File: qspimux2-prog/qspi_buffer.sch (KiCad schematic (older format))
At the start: 31 parts, among them J201 Conn_01x10_MountingPin, U201 SN74LVC1T45DCK, U202 SN74LVC1T45DCK, U203 SN74LVC1T45DCK, U204 SN74LVC1T45DCK, U205 SN74LVC1T45DCK, U206 SN74LVC1T45DCK, U207 SN74LVC1T45DCK

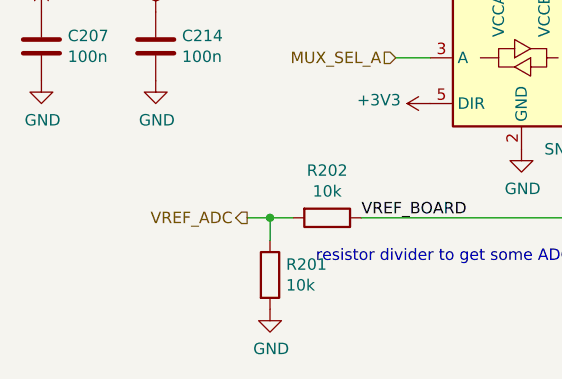
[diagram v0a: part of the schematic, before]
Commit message: add a few missing capacitors and do some slight layout optimizations
add two missing capacitors on the supply rails of the microcontroller
add capacitor to vtarget monitoringto get a low pass
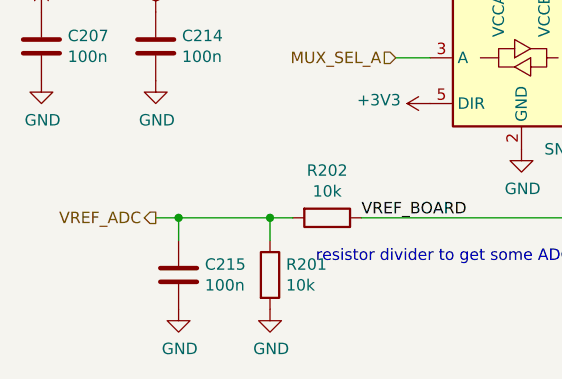
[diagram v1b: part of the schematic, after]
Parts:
- added C215: 100n, Capacitor_SMD:C_0402_1005Metric, symbol Device:C
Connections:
- net GND: now also C215.2
- net VREF_ADC: now also C215.1
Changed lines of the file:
@@
 $EndDescr
 $Comp
-L power:+3V3 #PWR0236
+L power:+3V3 #PWR0237
 U 1 1 5DE94518
 P 8300 5100
-F 0 "#PWR0236" H 8300 4950 50  0001 C CNN
+F 0 "#PWR0237" H 8300 4950 50  0001 C CNN
 F 1 "+3V3" H 8315 5273 50  0000 C CNN
 F 2 "" H 8300 5100 50  0001 C CNN
@@
 $EndComp
 $Comp
-L power:+3V3 #PWR0233
+L power:+3V3 #PWR0234
 U 1 1 5DE8F4FA
 P 8300 1200
-F 0 "#PWR0233" H 8300 1050 50  0001 C CNN
+F 0 "#PWR0234" H 8300 1050 50  0001 C CNN
 F 1 "+3V3" H 8315 1373 50  0000 C CNN
 F 2 "" H 8300 1200 50  0001 C CNN
@@
 $EndComp
 $Comp
-L power:VDD #PWR0253
+L power:VDD #PWR0254
 U 1 1 5DE9D1E1
 P 8500 9000
-F 0 "#PWR0253" H 8500 8850 50  0001 C CNN
+F 0 "#PWR0254" H 8500 8850 50  0001 C CNN
 F 1 "VDD" H 8517 9173 50  0000 C CNN
 F 2 "" H 8500 9000 50  0001 C CNN
@@
 $EndComp
 $Comp
-L power:+3V3 #PWR0234
+L power:+3V3 #PWR0235
 U 1 1 5DE91572
 P 8300 2500
-F 0 "#PWR0234" H 8300 2350 50  0001 C CNN
+F 0 "#PWR0235" H 8300 2350 50  0001 C CNN
 F 1 "+3V3" H 8315 2673 50  0000 C CNN
 F 2 "" H 8300 2500 50  0001 C CNN
@@
 $EndComp
 $Comp
-L power:VDD #PWR0252
+L power:VDD #PWR0253
 U 1 1 5DE99677
 P 8500 7700
-F 0 "#PWR0252" H 8500 7550 50  0001 C CNN
+F 0 "#PWR0253" H 8500 7550 50  0001 C CNN
 F 1 "VDD" H 8517 7873 50  0000 C CNN
 F 2 "" H 8500 7700 50  0001 C CNN
@@
 $EndComp
 $Comp
-L power:GND #PWR0241
+L power:GND #PWR0242
 U 1 1 5DEB0DC4
 P 8400 3300
-F 0 "#PWR0241" H 8400 3050 50  0001 C CNN
+F 0 "#PWR0242" H 8400 3050 50  0001 C CNN
 F 1 "GND" H 8405 3127 50  0000 C CNN
 F 2 "" H 8400 3300 50  0001 C CNN
@@
 $EndComp
 $Comp
-L power:GND #PWR0244
+L power:GND #PWR0245
 U 1 1 5E26BF26
 P 8400 7200
-F 0 "#PWR0244" H 8400 6950 50  0001 C CNN
+F 0 "#PWR0245" H 8400 6950 50  0001 C CNN
 F 1 "GND" H 8405 7027 50  0000 C CNN
 F 2 "" H 8400 7200 50  0001 C CNN
@@
 $EndComp
 $Comp
-L power:VDD #PWR0249
+L power:VDD #PWR0250
 U 1 1 5DE9300A
 P 8500 3800
-F 0 "#PWR0249" H 8500 3650 50  0001 C CNN
+F 0 "#PWR0250" H 8500 3650 50  0001 C CNN
 F 1 "VDD" H 8517 3973 50  0000 C CNN
 F 2 "" H 8500 3800 50  0001 C CNN
@@
 $EndComp
 $Comp
-L power:+3V3 #PWR0235
+L power:+3V3 #PWR0236
 U 1 1 5DE92FFC
 P 8300 3800
-F 0 "#PWR0235" H 8300 3650 50  0001 C CNN
+F 0 "#PWR0236" H 8300 3650 50  0001 C CNN
 F 1 "+3V3" H 8315 3973 50  0000 C CNN
 F 2 "" H 8300 3800 50  0001 C CNN
@@
 $EndComp
 $Comp
-L power:GND #PWR0242
+L power:GND #PWR0243
 U 1 1 5DEB8F33
 P 8400 4600
-F 0 "#PWR0242" H 8400 4350 50  0001 C CNN
+F 0 "#PWR0243" H 8400 4350 50  0001 C CNN
 F 1 "GND" H 8405 4427 50  0000 C CNN
 F 2 "" H 8400 4600 50  0001 C CNN
@@
 $EndComp
 $Comp
-L power:VDD #PWR0247
+L power:VDD #PWR0248
 U 1 1 5DE90785
 P 8500 1200
-F 0 "#PWR0247" H 8500 1050 50  0001 C CNN
+F 0 "#PWR0248" H 8500 1050 50  0001 C CNN
 F 1 "VDD" H 8517 1373 50  0000 C CNN
 F 2 "" H 8500 1200 50  0001 C CNN
@@
 $EndComp
 $Comp
-L power:+3V3 #PWR0237
+L power:+3V3 #PWR0238
 U 1 1 5DE971AE
 P 8300 6400
-F 0 "#PWR0237" H 8300 6250 50  0001 C CNN
+F 0 "#PWR0238" H 8300 6250 50  0001 C CNN
 F 1 "+3V3" H 8315 6573 50  0000 C CNN
 F 2 "" H 8300 6400 50  0001 C CNN
@@
 $EndComp
 $Comp
-L power:VDD #PWR0248
+L power:VDD #PWR0249
 U 1 1 5DE91580
 P 8500 2500
-F 0 "#PWR0248" H 8500 2350 50  0001 C CNN
+F 0 "#PWR0249" H 8500 2350 50  0001 C CNN
 F 1 "VDD" H 8517 2673 50  0000 C CNN
 F 2 "" H 8500 2500 50  0001 C CNN
@@
 $EndComp
 $Comp
-L power:GND #PWR0240
+L power:GND #PWR0241
 U 1 1 5DE8B08B
 P 8400 2000
-F 0 "#PWR0240" H 8400 1750 50  0001 C CNN
+F 0 "#PWR0241" H 8400 1750 50  0001 C CNN
 F 1 "GND" H 8405 1827 50  0000 C CNN
 F 2 "" H 8400 2000 50  0001 C CNN
@@
 $EndComp
 $Comp
-L power:VDD #PWR0250
+L power:VDD #PWR0251
 U 1 1 5DE94526
 P 8500 5100
-F 0 "#PWR0250" H 8500 4950 50  0001 C CNN
+F 0 "#PWR0251" H 8500 4950 50  0001 C CNN
 F 1 "VDD" H 8517 5273 50  0000 C CNN
 F 2 "" H 8500 5100 50  0001 C CNN
@@
 $EndComp
 $Comp
-L power:GND #PWR0243
+L power:GND #PWR0244
 U 1 1 5DEB94D5
 P 8400 5900
-F 0 "#PWR0243" H 8400 5650 50  0001 C CNN
+F 0 "#PWR0244" H 8400 5650 50  0001 C CNN
 F 1 "GND" H 8405 5727 50  0000 C CNN
 F 2 "" H 8400 5900 50  0001 C CNN
@@
 $EndComp
 $Comp
-L power:GND #PWR0245
+L power:GND #PWR0246
 U 1 1 5DEC9D31
 P 8400 8500
-F 0 "#PWR0245" H 8400 8250 50  0001 C CNN
+F 0 "#PWR0246" H 8400 8250 50  0001 C CNN
 F 1 "GND" H 8405 8327 50  0000 C CNN
 F 2 "" H 8400 8500 50  0001 C CNN
@@
 $EndComp
 $Comp
-L power:VDD #PWR0251
+L power:VDD #PWR0252
 U 1 1 5DE971BC
 P 8500 6400
-F 0 "#PWR0251" H 8500 6250 50  0001 C CNN
+F 0 "#PWR0252" H 8500 6250 50  0001 C CNN
 F 1 "VDD" H 8517 6573 50  0000 C CNN
 F 2 "" H 8500 6400 50  0001 C CNN
@@
 $EndComp
 $Comp
-L power:+3V3 #PWR0238
+L power:+3V3 #PWR0239
 U 1 1 5DE99669
 P 8300 7700
-F 0 "#PWR0238" H 8300 7550 50  0001 C CNN
+F 0 "#PWR0239" H 8300 7550 50  0001 C CNN
 F 1 "+3V3" H 8315 7873 50  0000 C CNN
 F 2 "" H 8300 7700 50  0001 C CNN
@@
 $EndComp
 $Comp
-L power:GND #PWR0246
+L power:GND #PWR0247
 U 1 1 5DECAA79
 P 8400 9800
-F 0 "#PWR0246" H 8400 9550 50  0001 C CNN
+F 0 "#PWR0247" H 8400 9550 50  0001 C CNN
 F 1 "GND" H 8405 9627 50  0000 C CNN
 F 2 "" H 8400 9800 50  0001 C CNN
@@
 $EndComp
 $Comp
-L power:+3V3 #PWR0239
+L power:+3V3 #PWR0240
 U 1 1 5DE9D1D3
 P 8300 9000
-F 0 "#PWR0239" H 8300 8850 50  0001 C CNN
+F 0 "#PWR0240" H 8300 8850 50  0001 C CNN
 F 1 "+3V3" H 8315 9173 50  0000 C CNN
 F 2 "" H 8300 9000 50  0001 C CNN
@@
 $EndComp
 $Comp
-L power:+3V3 #PWR0232
+L power:+3V3 #PWR0233
 U 1 1 5E06B1B2
 P 8000 9600
-F 0 "#PWR0232" H 8000 9450 50  0001 C CNN
+F 0 "#PWR0233" H 8000 9450 50  0001 C CNN
 F 1 "+3V3" V 8015 9728 50  0000 L CNN
 F 2 "" H 8000 9600 50  0001 C CNN
@@
 $EndComp
 $Comp
-L power:+3V3 #PWR0230
+L power:+3V3 #PWR0231
 U 1 1 5E054678
 P 8000 1800
-F 0 "#PWR0230" H 8000 1650 50  0001 C CNN
+F 0 "#PWR0231" H 8000 1650 50  0001 C CNN
 F 1 "+3V3" V 8015 1928 50  0000 L CNN
 F 2 "" H 8000 1800 50  0001 C CNN
@@
 $EndComp
 $Comp
-L power:GND #PWR0229
+L power:GND #PWR0230
 U 1 1 5E230D27
 P 7300 10500
-F 0 "#PWR0229" H 7300 10250 50  0001 C CNN
+F 0 "#PWR0230" H 7300 10250 50  0001 C CNN
 F 1 "GND" H 7305 10327 50  0000 C CNN
 F 2 "" H 7300 10500 50  0001 C CNN
@@
 	10400 10100 7700 10100
 Wire Wire Line
-	7200 10100 7300 10100
+	6800 10100 6900 10100
 Wire Wire Line
 	7900 8300 8000 8300
@@
 $EndComp
 $Comp
-L power:GND #PWR0256
+L power:GND #PWR0257
 U 1 1 5DEECC05
 P 11200 6900
-F 0 "#PWR0256" H 11200 6650 50  0001 C CNN
+F 0 "#PWR0257" H 11200 6650 50  0001 C CNN
 F 1 "GND" H 11205 6727 50  0000 C CNN
 F 2 "" H 11200 6900 50  0001 C CNN
@@
 $EndComp
 $Comp
-L power:+3V3 #PWR0231
+L power:+3V3 #PWR0232
 U 1 1 5E053733
 P 8000 7000
-F 0 "#PWR0231" H 8000 6850 50  0001 C CNN
+F 0 "#PWR0232" H 8000 6850 50  0001 C CNN
 F 1 "+3V3" V 8015 7128 50  0000 L CNN
 F 2 "" H 8000 7000 50  0001 C CNN
@@
 $EndComp
 $Comp
-L power:GND #PWR0255
+L power:GND #PWR0256
 U 1 1 5DF27FD6
 P 10900 6900
-F 0 "#PWR0255" H 10900 6650 50  0001 C CNN
+F 0 "#PWR0256" H 10900 6650 50  0001 C CNN
 F 1 "GND" H 10905 6727 50  0000 C CNN
 F 2 "" H 10900 6900 50  0001 C CNN
@@
 $EndComp
 $Comp
-L power:VDD #PWR0254
+L power:VDD #PWR0255
 U 1 1 5DF09489
 P 10900 5700
-F 0 "#PWR0254" H 10900 5550 50  0001 C CNN
+F 0 "#PWR0255" H 10900 5550 50  0001 C CNN
 F 1 "VDD" H 10917 5873 50  0000 C CNN
 F 2 "" H 10900 5700 50  0001 C CNN
@@
 Text HLabel 7850 9400 0    50   Input ~ 0
 MUX_SEL_A
-Text HLabel 7200 10100 0    50   Output ~ 0
+Text HLabel 6800 10100 0    50   Output ~ 0
 VREF_ADC
 $Comp
@@
 	1    0    0    -1
 $EndComp
+$Comp
+L Device:C C215
+U 1 1 5E066B28
+P 6900 10350
+F 0 "C215" H 7015 10396 50  0000 L CNN
+F 1 "100n" H 7015 10305 50  0000 L CNN
+F 2 "Capacitor_SMD:C_0402_1005Metric" H 6938 10200 50  0001 C CNN
+F 3 "~" H 6900 10350 50  0001 C CNN
+	1    6900 10350
+	1    0    0    -1
+$EndComp
+$Comp
+L power:GND #PWR0229
+U 1 1 5E066B35
+P 6900 10500
+F 0 "#PWR0229" H 6900 10250 50  0001 C CNN
+F 1 "GND" H 6905 10327 50  0000 C CNN
+F 2 "" H 6900 10500 50  0001 C CNN
+F 3 "" H 6900 10500 50  0001 C CNN
+	1    6900 10500
+	1    0    0    -1
+$EndComp
+Wire Wire Line
+	6900 10200 6900 10100
+Connection ~ 6900 10100
+Wire Wire Line
+	6900 10100 7300 10100
 $EndSCHEMATC
